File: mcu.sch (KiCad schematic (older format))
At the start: 20 parts, among them P1 FLASH_HDR, P2 CONN_01X06, P3 USB_OTG, P4 CONN_01X04, U1 MK20DX256VLH7, X1 CRYSTAL_SMD

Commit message: Switched to different Debug Ports
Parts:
- added P5: CONN_01X02, lib.pretty:Conn-2, symbol CONN_01X02
- P2: footprint Pin_Headers:Pin_Header_Straight_1x06_Pitch2.00mm -> lib.pretty:Conn-6
- P4: footprint Pin_Headers:Pin_Header_Straight_1x04_Pitch2.00mm -> lib.pretty:Conn-4
- S72: footprint lib.pretty:TACT_5.2x5.2 -> lib.pretty:PTS810
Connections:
- net PTE1 renamed RX1
- net RX1: now also P5.2 (P2)
- net PTE2 renamed TX1
- net TX1: now also P5.1 (P1)
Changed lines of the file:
@@
 F 0 "S72" H 8725 3875 50  0000 L BNN
 F 1 "TAC_SWITCH" H 8525 3450 50  0000 L BNN
-F 2 "lib.pretty:TACT_5.2x5.2" H 8750 3800 50  0001 C CNN
+F 2 "lib.pretty:PTS810" H 8750 3800 50  0001 C CNN
 F 3 "" H 8750 3650 60  0000 C CNN
 	1    8750 3650
@@
 F 0 "P4" H 3150 1300 50  0000 C CNN
 F 1 "CONN_01X04" V 3250 1050 50  0000 C CNN
-F 2 "Pin_Headers:Pin_Header_Straight_1x04_Pitch2.00mm" H 3150 1050 50  0001 C CNN
+F 2 "lib.pretty:Conn-4" H 3150 1050 50  0001 C CNN
 F 3 "" H 3150 1050 50  0000 C CNN
 	1    3150 1050
@@
 	0    -1   -1   0
 $EndComp
-Text HLabel 4900 2250 0    40   3State ~ 0
-PTE1
-Text HLabel 4900 2350 0    40   3State ~ 0
-PTE2
 $Comp
 L +5V #PWR044
@@
 F 0 "P2" H 3950 1400 50  0000 C CNN
 F 1 "CONN_01X06" V 4050 1050 50  0000 C CNN
-F 2 "Pin_Headers:Pin_Header_Straight_1x06_Pitch2.00mm" H 3950 1050 50  0001 C CNN
+F 2 "lib.pretty:Conn-6" H 3950 1050 50  0001 C CNN
 F 3 "" H 3950 1050 50  0000 C CNN
 	1    3950 1050
@@
 Wire Wire Line
 	1650 1050 1600 1050
+Text Label 4900 2250 2    39   ~ 0
+RX1
+Text Label 4900 2350 2    39   ~ 0
+TX1
+$Comp
+L CONN_01X02 P5
+U 1 1 5789F16B
+P 4600 1050
+F 0 "P5" H 4600 1200 50  0000 C CNN
+F 1 "CONN_01X02" V 4700 1050 50  0000 C CNN
+F 2 "lib.pretty:Conn-2" H 4600 1050 50  0001 C CNN
+F 3 "" H 4600 1050 50  0000 C CNN
+	1    4600 1050
+	1    0    0    -1
+$EndComp
+Text Label 4400 1100 2    39   ~ 0
+RX1
+Text Label 4400 1000 2    39   ~ 0
+TX1
 $EndSCHEMATC

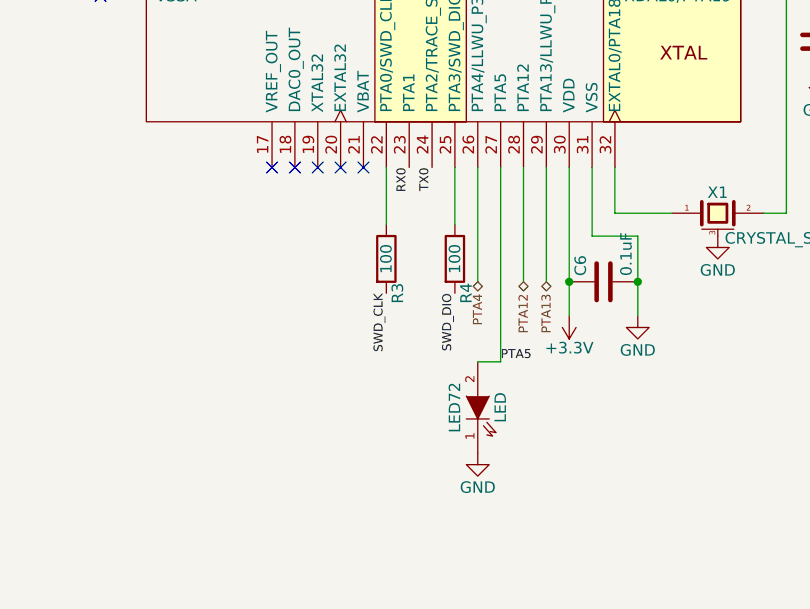
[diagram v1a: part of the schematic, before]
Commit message: Addressed the Points raised in Issue #2
Added Resistor to ground for firmware-LED
Connect VBAT to 3.3V
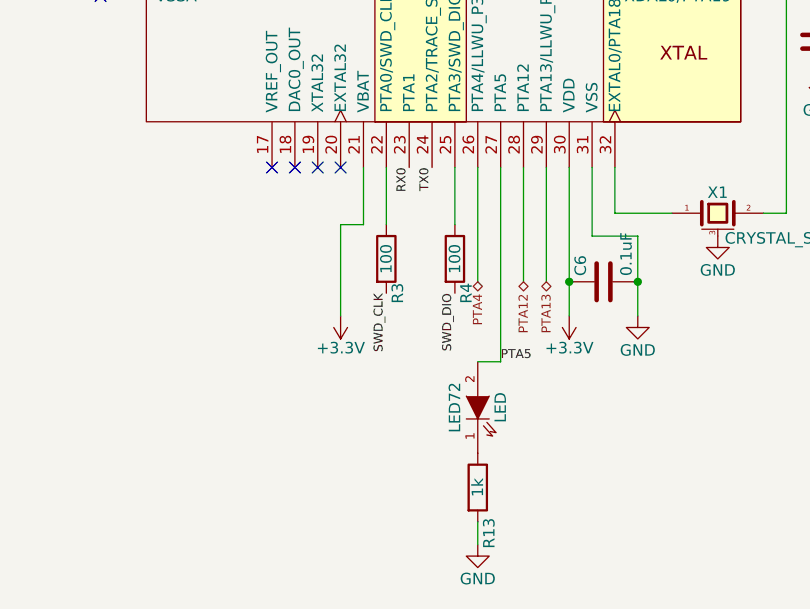
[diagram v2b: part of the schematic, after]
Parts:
- added R13: 1k, Resistors_SMD:R_0603, symbol R
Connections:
- net +3V3: now also U1.21 (VBAT)
- net GND: now also R13.2; no longer LED72.1 (K)
- new net: LED72.1 (K), R13.1
- no-connect marks 18 -> 17
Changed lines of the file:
@@
 USB_D-
 $Comp
-L +5V #PWR024
+L +5V #PWR26
 U 1 1 575CB90E
 P 2050 850
-F 0 "#PWR024" H 2050 700 50  0001 C CNN
+F 0 "#PWR26" H 2050 700 50  0001 C CNN
 F 1 "+5V" H 2050 990 50  0000 C CNN
 F 2 "" H 2050 850 50  0000 C CNN
@@
 $EndComp
 $Comp
-L GND #PWR025
+L GND #PWR30
 U 1 1 575CB946
 P 2900 1250
-F 0 "#PWR025" H 2900 1000 50  0001 C CNN
+F 0 "#PWR30" H 2900 1000 50  0001 C CNN
 F 1 "GND" H 2900 1100 50  0000 C CNN
 F 2 "" H 2900 1250 50  0000 C CNN
@@
 $EndComp
 $Comp
-L GND #PWR026
+L GND #PWR46
 U 1 1 575D1056
-P 6550 5750
-F 0 "#PWR026" H 6550 5500 50  0001 C CNN
-F 1 "GND" H 6550 5600 50  0000 C CNN
-F 2 "" H 6550 5750 50  0000 C CNN
-F 3 "" H 6550 5750 50  0000 C CNN
-	1    6550 5750
+P 6550 6150
+F 0 "#PWR46" H 6550 5900 50  0001 C CNN
+F 1 "GND" H 6550 6000 50  0000 C CNN
+F 2 "" H 6550 6150 50  0000 C CNN
+F 3 "" H 6550 6150 50  0000 C CNN
+	1    6550 6150
 	1    0    0    -1
 $EndComp
@@
 NoConn ~ 4900 3150
 NoConn ~ 4900 3050
-NoConn ~ 6050 4500
 $Comp
 L LED LED72
@@
 $EndComp
 $Comp
-L GND #PWR027
+L GND #PWR42
 U 1 1 575C7BBF
 P 7600 4800
-F 0 "#PWR027" H 7600 4550 50  0001 C CNN
+F 0 "#PWR42" H 7600 4550 50  0001 C CNN
 F 1 "GND" H 7600 4650 50  0000 C CNN
 F 2 "" H 7600 4800 50  0000 C CNN
@@
 $EndComp
 $Comp
-L GND #PWR028
+L GND #PWR45
 U 1 1 575C810A
 P 7250 5150
-F 0 "#PWR028" H 7250 4900 50  0001 C CNN
+F 0 "#PWR45" H 7250 4900 50  0001 C CNN
 F 1 "GND" H 7250 5000 50  0000 C CNN
 F 2 "" H 7250 5150 50  0000 C CNN
@@
 $EndComp
 $Comp
-L GND #PWR029
+L GND #PWR40
 U 1 1 575C868D
 P 9050 3850
-F 0 "#PWR029" H 9050 3600 50  0001 C CNN
+F 0 "#PWR40" H 9050 3600 50  0001 C CNN
 F 1 "GND" H 9050 3700 50  0000 C CNN
 F 2 "" H 9050 3850 50  0000 C CNN
@@
 $EndComp
 $Comp
-L GND #PWR030
+L GND #PWR41
 U 1 1 575C9201
 P 8050 4100
-F 0 "#PWR030" H 8050 3850 50  0001 C CNN
+F 0 "#PWR41" H 8050 3850 50  0001 C CNN
 F 1 "GND" H 8050 3950 50  0000 C CNN
 F 2 "" H 8050 4100 50  0000 C CNN
@@
 $EndComp
 $Comp
-L GND #PWR031
+L GND #PWR35
 U 1 1 575C9D7B
 P 8400 2350
-F 0 "#PWR031" H 8400 2100 50  0001 C CNN
+F 0 "#PWR35" H 8400 2100 50  0001 C CNN
 F 1 "GND" H 8400 2200 50  0000 C CNN
 F 2 "" H 8400 2350 50  0000 C CNN
@@
 $EndComp
 $Comp
-L +3.3V #PWR032
+L +3.3V #PWR33
 U 1 1 575CA307
 P 8150 2050
-F 0 "#PWR032" H 8150 1900 50  0001 C CNN
+F 0 "#PWR33" H 8150 1900 50  0001 C CNN
 F 1 "+3.3V" H 8150 2190 50  0000 C CNN
 F 2 "" H 8150 2050 50  0000 C CNN
@@
 $EndComp
 $Comp
-L GND #PWR033
+L GND #PWR36
 U 1 1 575CA5B6
 P 4400 2550
-F 0 "#PWR033" H 4400 2300 50  0001 C CNN
+F 0 "#PWR36" H 4400 2300 50  0001 C CNN
 F 1 "GND" H 4400 2400 50  0000 C CNN
 F 2 "" H 4400 2550 50  0000 C CNN
@@
 $EndComp
 $Comp
-L +3.3V #PWR034
+L +3.3V #PWR34
 U 1 1 575CAD2D
 P 4400 2250
-F 0 "#PWR034" H 4400 2100 50  0001 C CNN
+F 0 "#PWR34" H 4400 2100 50  0001 C CNN
 F 1 "+3.3V" H 4400 2390 50  0000 C CNN
 F 2 "" H 4400 2250 50  0000 C CNN
@@
 $EndComp
 $Comp
-L +3.3V #PWR035
+L +3.3V #PWR44
 U 1 1 575CB558
 P 6950 5150
-F 0 "#PWR035" H 6950 5000 50  0001 C CNN
+F 0 "#PWR44" H 6950 5000 50  0001 C CNN
 F 1 "+3.3V" H 6950 5290 50  0000 C CNN
 F 2 "" H 6950 5150 50  0000 C CNN
@@
 $EndComp
 $Comp
-L GND #PWR036
+L GND #PWR39
 U 1 1 575CD528
 P 4400 3550
-F 0 "#PWR036" H 4400 3300 50  0001 C CNN
+F 0 "#PWR39" H 4400 3300 50  0001 C CNN
 F 1 "GND" H 4400 3400 50  0000 C CNN
 F 2 "" H 4400 3550 50  0000 C CNN
@@
 $EndComp
 $Comp
-L +3.3V #PWR037
+L +3.3V #PWR37
 U 1 1 575CD770
 P 4200 2850
-F 0 "#PWR037" H 4200 2700 50  0001 C CNN
+F 0 "#PWR37" H 4200 2700 50  0001 C CNN
 F 1 "+3.3V" H 4200 2990 50  0000 C CNN
 F 2 "" H 4200 2850 50  0000 C CNN
@@
 $EndComp
 $Comp
-L +5V #PWR038
+L +5V #PWR38
 U 1 1 575CD8E4
 P 4550 2950
-F 0 "#PWR038" H 4550 2800 50  0001 C CNN
+F 0 "#PWR38" H 4550 2800 50  0001 C CNN
 F 1 "+5V" H 4550 3090 50  0000 C CNN
 F 2 "" H 4550 2950 50  0000 C CNN
@@
 $EndComp
 $Comp
-L +3.3V #PWR039
+L +3.3V #PWR25
 U 1 1 575D0650
 P 9800 750
-F 0 "#PWR039" H 9800 600 50  0001 C CNN
+F 0 "#PWR25" H 9800 600 50  0001 C CNN
 F 1 "+3.3V" H 9800 890 50  0000 C CNN
 F 2 "" H 9800 750 50  0000 C CNN
@@
 $EndComp
 $Comp
-L GND #PWR040
+L GND #PWR31
 U 1 1 575D069B
 P 9600 1450
-F 0 "#PWR040" H 9600 1200 50  0001 C CNN
+F 0 "#PWR31" H 9600 1200 50  0001 C CNN
 F 1 "GND" H 9600 1300 50  0000 C CNN
 F 2 "" H 9600 1450 50  0000 C CNN
@@
 $EndComp
 $Comp
-L +5V #PWR041
+L +5V #PWR32
 U 1 1 575D1514
 P 9800 1450
-F 0 "#PWR041" H 9800 1300 50  0001 C CNN
+F 0 "#PWR32" H 9800 1300 50  0001 C CNN
 F 1 "+5V" H 9800 1590 50  0000 C CNN
 F 2 "" H 9800 1450 50  0000 C CNN
@@
 USB_D-
 $Comp
-L +5V #PWR042
+L +5V #PWR27
 U 1 1 575E7A49
 P 2900 850
-F 0 "#PWR042" H 2900 700 50  0001 C CNN
+F 0 "#PWR27" H 2900 700 50  0001 C CNN
 F 1 "+5V" H 2900 990 50  0000 C CNN
 F 2 "" H 2900 850 50  0000 C CNN
@@
 $EndComp
 $Comp
-L GND #PWR043
+L GND #PWR29
 U 1 1 575E7A8D
 P 2050 1250
-F 0 "#PWR043" H 2050 1000 50  0001 C CNN
+F 0 "#PWR29" H 2050 1000 50  0001 C CNN
 F 1 "GND" H 2050 1100 50  0000 C CNN
 F 2 "" H 2050 1250 50  0000 C CNN
@@
 $EndComp
 $Comp
-L +5V #PWR044
+L +5V #PWR24
 U 1 1 57883411
 P 3700 750
-F 0 "#PWR044" H 3700 600 50  0001 C CNN
+F 0 "#PWR24" H 3700 600 50  0001 C CNN
 F 1 "+5V" H 3700 890 50  0000 C CNN
 F 2 "" H 3700 750 50  0000 C CNN
@@
 SWD_CLK
 $Comp
-L GND #PWR045
+L GND #PWR28
 U 1 1 57884050
 P 3550 1100
-F 0 "#PWR045" H 3550 850 50  0001 C CNN
+F 0 "#PWR28" H 3550 850 50  0001 C CNN
 F 1 "GND" H 3550 950 50  0000 C CNN
 F 2 "" H 3550 1100 50  0000 C CNN
@@
 Text Label 4400 1000 2    39   ~ 0
 TX1
+$Comp
+L +3.3V #PWR43
+U 1 1 583F6182
+P 5950 5150
+F 0 "#PWR43" H 5950 5000 50  0001 C CNN
+F 1 "+3.3V" H 5950 5290 50  0000 C CNN
+F 2 "" H 5950 5150 50  0000 C CNN
+F 3 "" H 5950 5150 50  0000 C CNN
+	1    5950 5150
+	-1   0    0    1
+$EndComp
+Wire Wire Line
+	6050 4500 6050 4750
+Wire Wire Line
+	6050 4750 5950 4750
+Wire Wire Line
+	5950 4750 5950 5150
+$Comp
+L R R13
+U 1 1 583F6DA0
+P 6550 5900
+F 0 "R13" V 6600 5700 50  0000 C CNN
+F 1 "1k" V 6550 5900 50  0000 C CNN
+F 2 "Resistors_SMD:R_0603" V 6480 5900 50  0001 C CNN
+F 3 "" H 6550 5900 50  0000 C CNN
+	1    6550 5900
+	1    0    0    -1
+$EndComp
+Wire Wire Line
+	6550 6050 6550 6150
 $EndSCHEMATC
